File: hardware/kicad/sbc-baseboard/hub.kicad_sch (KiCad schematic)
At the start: 84 parts, among them J1 USB-C upstream, J4 USB-A x2, J5 USB-A x2, U401 USBLC6-2SC6, U402 USB2517, U403 TPS2553DBV, U404 TPS2553DBV, U405 TPS2553DBV, U406 TPS2553DBV, U407 TPS2553DBV, U408 USBLC6-2SC6, U409 USBLC6-2SC6, U410 USBLC6-2SC6, U411 USBLC6-2SC6, Y401 24MHz

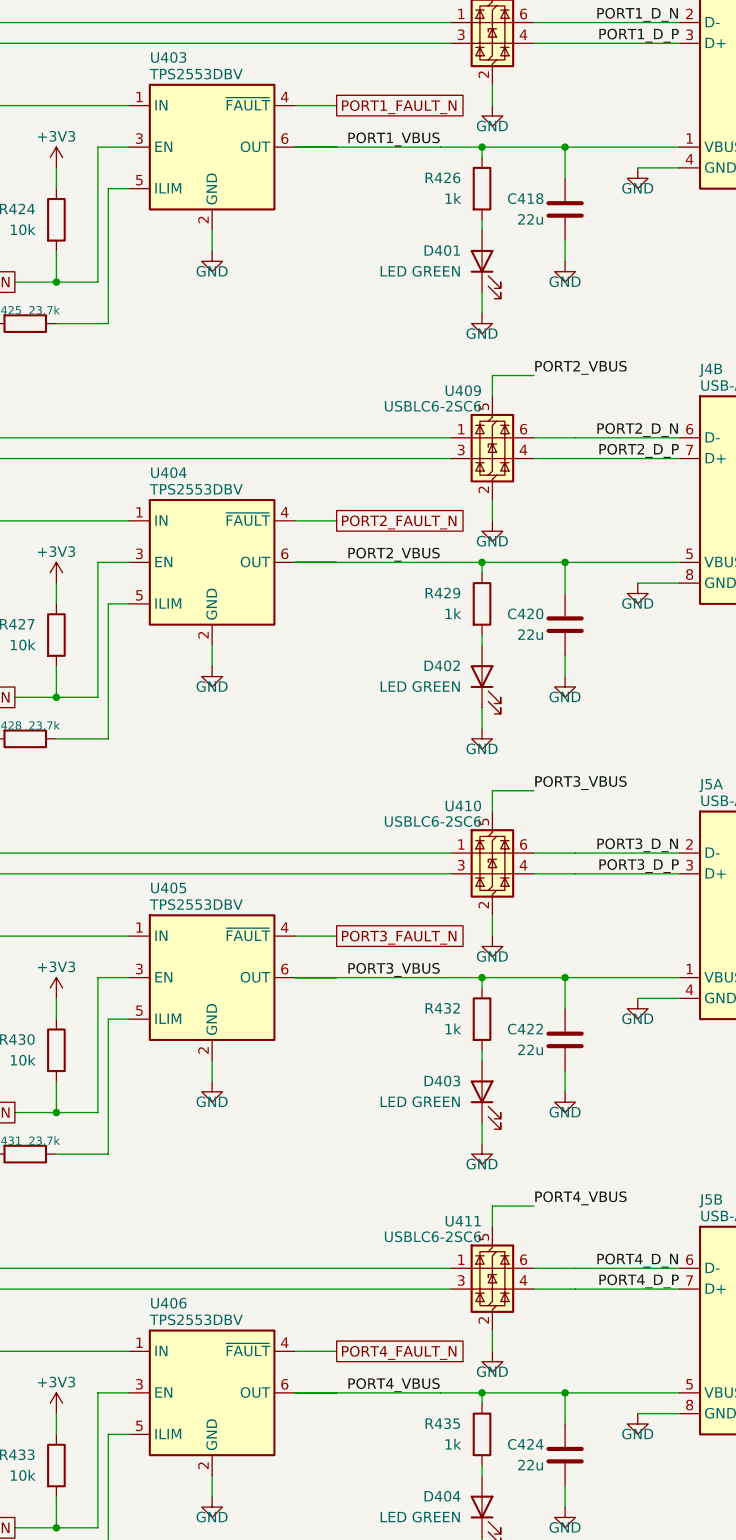
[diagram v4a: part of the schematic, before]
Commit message: Nothing drawn over anything else; FTDI Friend header; DAPLink per FRDM-K64F; 90 ohm USB class
Geometry gate now also reports two wires sharing a stretch, and is at zero on
every sheet. Routes into a stacked connector from one side take staggered
columns and rows; the signal relays are flipped so COM meets the header's
first pin without crossings; the opto-isolator moves above the passthrough
wires and taps the relay's COM lane; a tag before a route ends at the route's
target; routes into joined pins end at the join; the K64's VREGIN diode taps
the VBUS lane beside the ESD's stub; symbol mirrors are applied after
rotation, as KiCad does.

FT231X: the 3V3OUT lane stays on its pin row with its capacitor far out, clear
of the VCC decoupling; J9 mirrors the Adafruit FTDI Friend (VCC 5 V and pin 6
RTS by default on bridged solder jumpers; the first pass had left J9's VCC on
an open jumper only).

DAPLink K20, verified against DAPLink k20dx and the FRDM-K64F OpenSDA circuit:
PTC7 (SWDIO_IN) joins the SWDIO net, 33 R series resistors on the K20's USB
pair (K20_USB_P/N), notes and spec questions 12 and 14 resolved.

USB net class: 0.35 mm / 0.20 mm for 90 ohm on Advanced Circuits' standard
4-layer 62 mil stackup (spec section 8a). ERC 0, geometry 0, merges 0, layout
0, builds reproducible.

Co-Authored-By: Claude Fable 5.1 <noreply@anthropic.com>
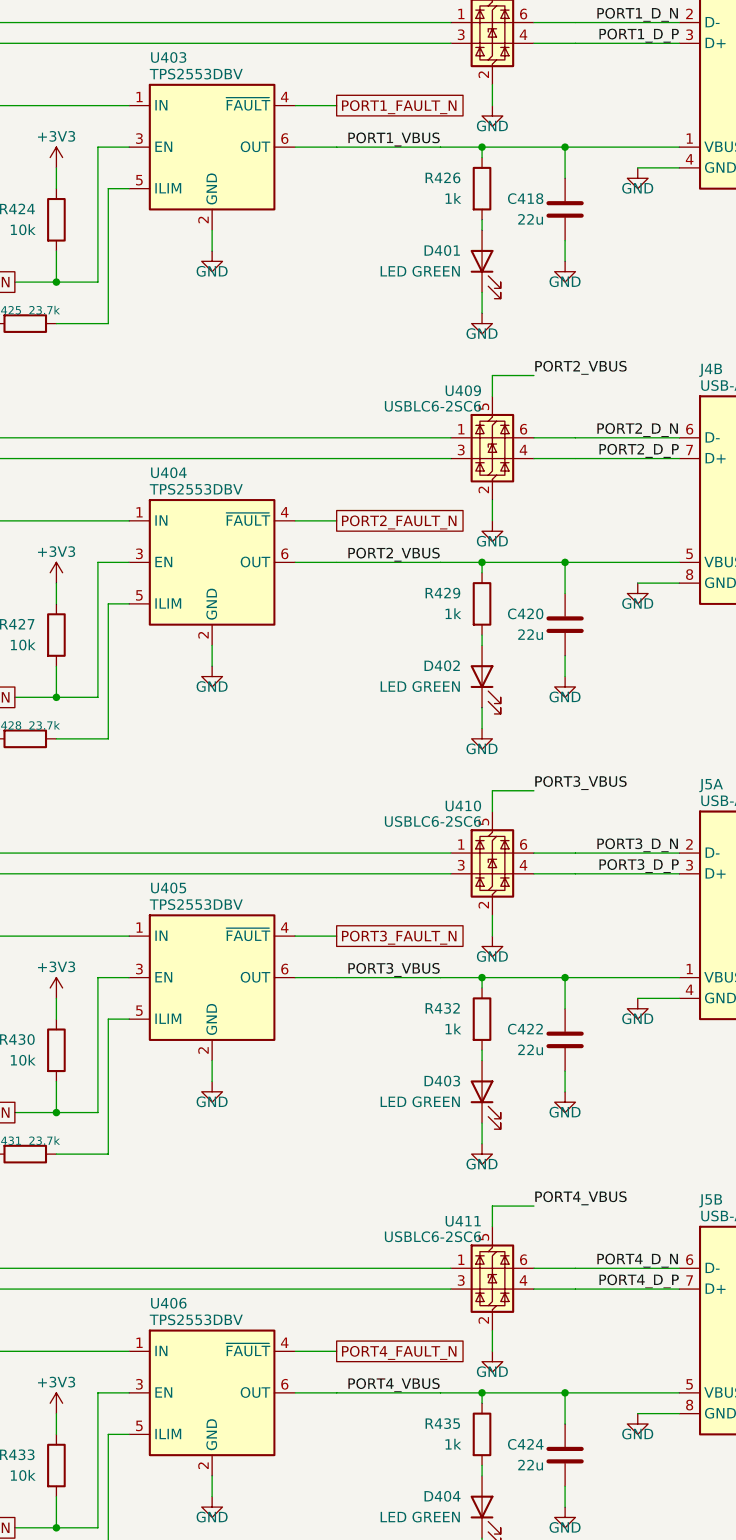
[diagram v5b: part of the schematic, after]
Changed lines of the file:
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@@
 		(pts
 			(xy 355.6 60.96)
-			(xy 337.82 60.96)
-		)
-		(stroke
-			(width 0)
-			(type default)
-		)
-	)
-	(wire
-		(pts
-			(xy 337.82 60.96)
 			(xy 342.9 60.96)
 		)
@@
 		(pts
 			(xy 355.6 111.76)
-			(xy 337.82 111.76)
-		)
-		(stroke
-			(width 0)
-			(type default)
-		)
-	)
-	(wire
-		(pts
-			(xy 337.82 111.76)
 			(xy 342.9 111.76)
 		)
@@
 		(pts
 			(xy 355.6 162.56)
-			(xy 337.82 162.56)
-		)
-		(stroke
-			(width 0)
-			(type default)
-		)
-	)
-	(wire
-		(pts
-			(xy 337.82 162.56)
 			(xy 342.9 162.56)
 		)
@@
 		(pts
 			(xy 355.6 213.36)
-			(xy 337.82 213.36)
-		)
-		(stroke
-			(width 0)
-			(type default)
-		)
-	)
-	(wire
-		(pts
-			(xy 337.82 213.36)
 			(xy 342.9 213.36)
 		)

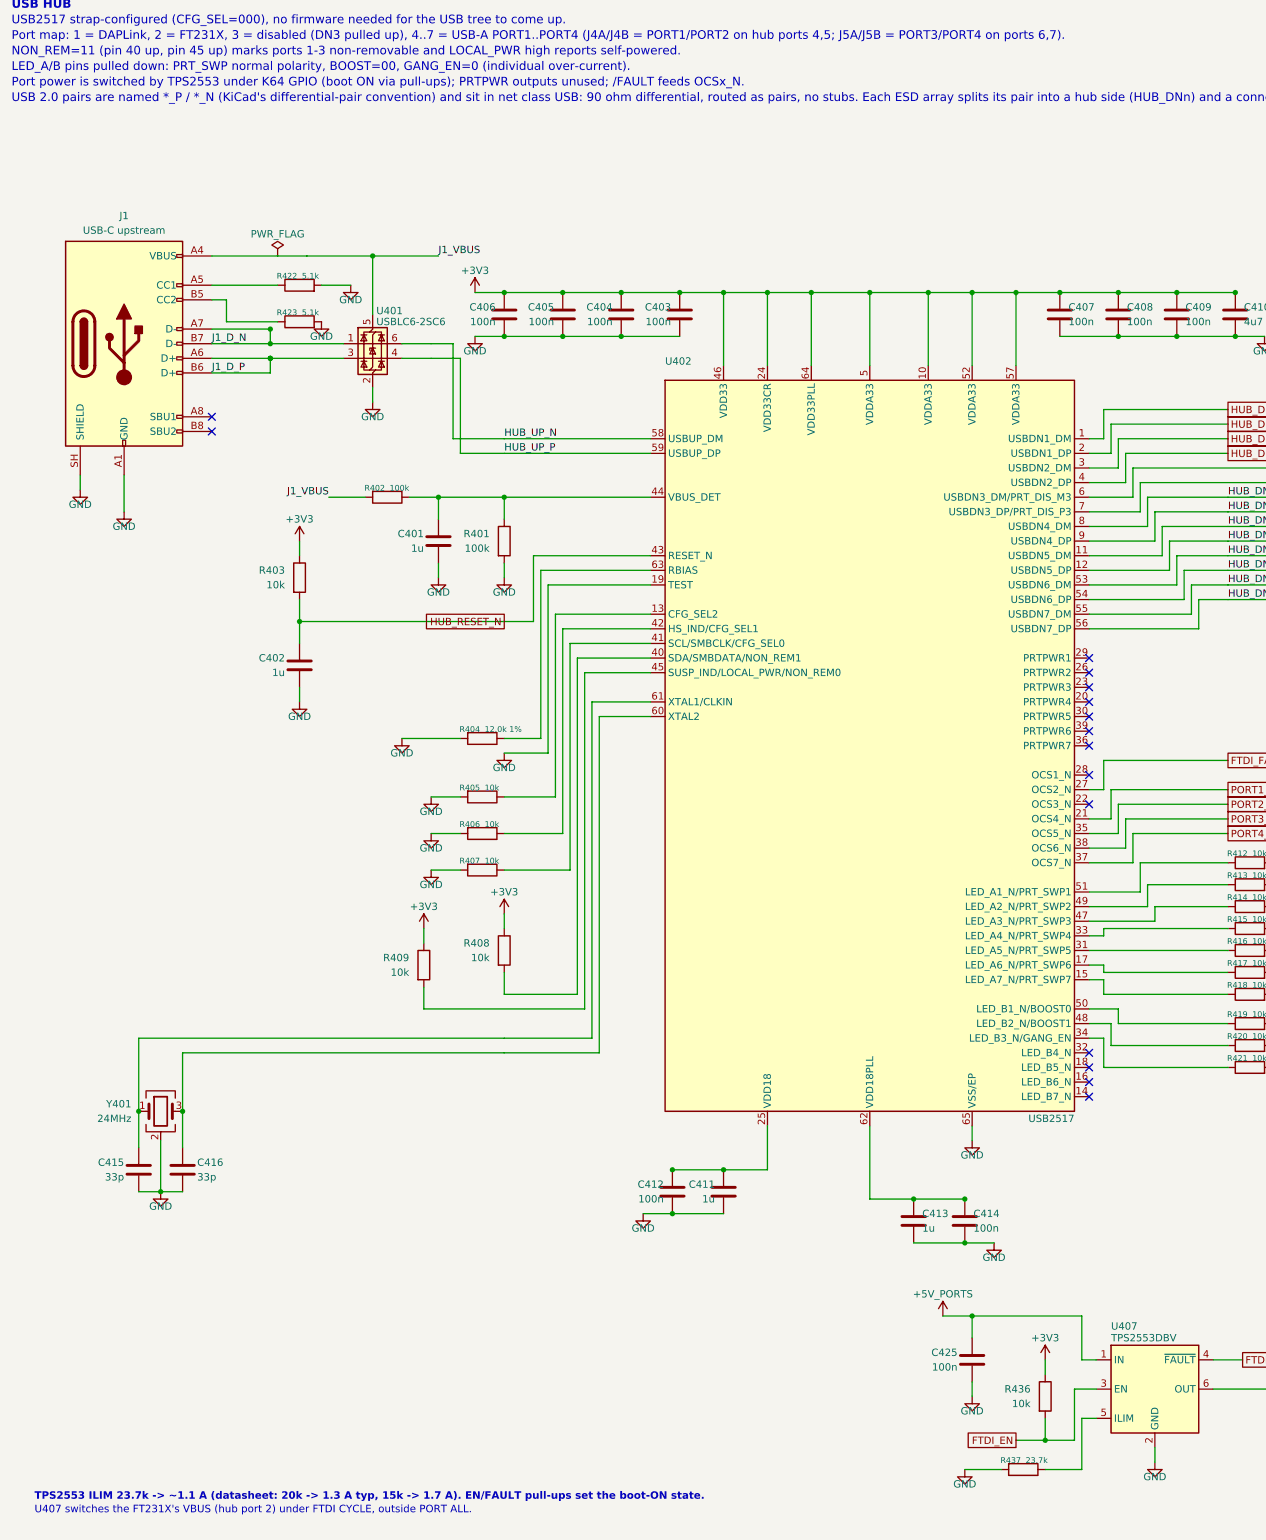
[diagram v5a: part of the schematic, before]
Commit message: Current pathways annotated on the sheets; net classes PSU_3A, USB_VBUS_3A, PWR_6A; layout directives
Net class directive flags on every high-current net, with the class name
carrying the current: the PSU passthrough (PSU_VP, PSU_VOUT, PSU_GND, now
named), the USB port and FTDI VBUS, VBUS_IN, and the +5V_PORTS / +5V_TGT rails
on the power sheet's flag strip. The project file carries the classes with
their widths and patterns; the XML netlist confirms every net's class. Sheet
notes state the currents and widths. Spec: FTDI header section rewritten for
the Adafruit FTDI Friend defaults (a deliberate exception to the back-feed
rule), current-pathway table in 8a. docs/layout-directives.md written from
the spec for the layout generator.

Co-Authored-By: Claude Fable 5.1 <noreply@anthropic.com>
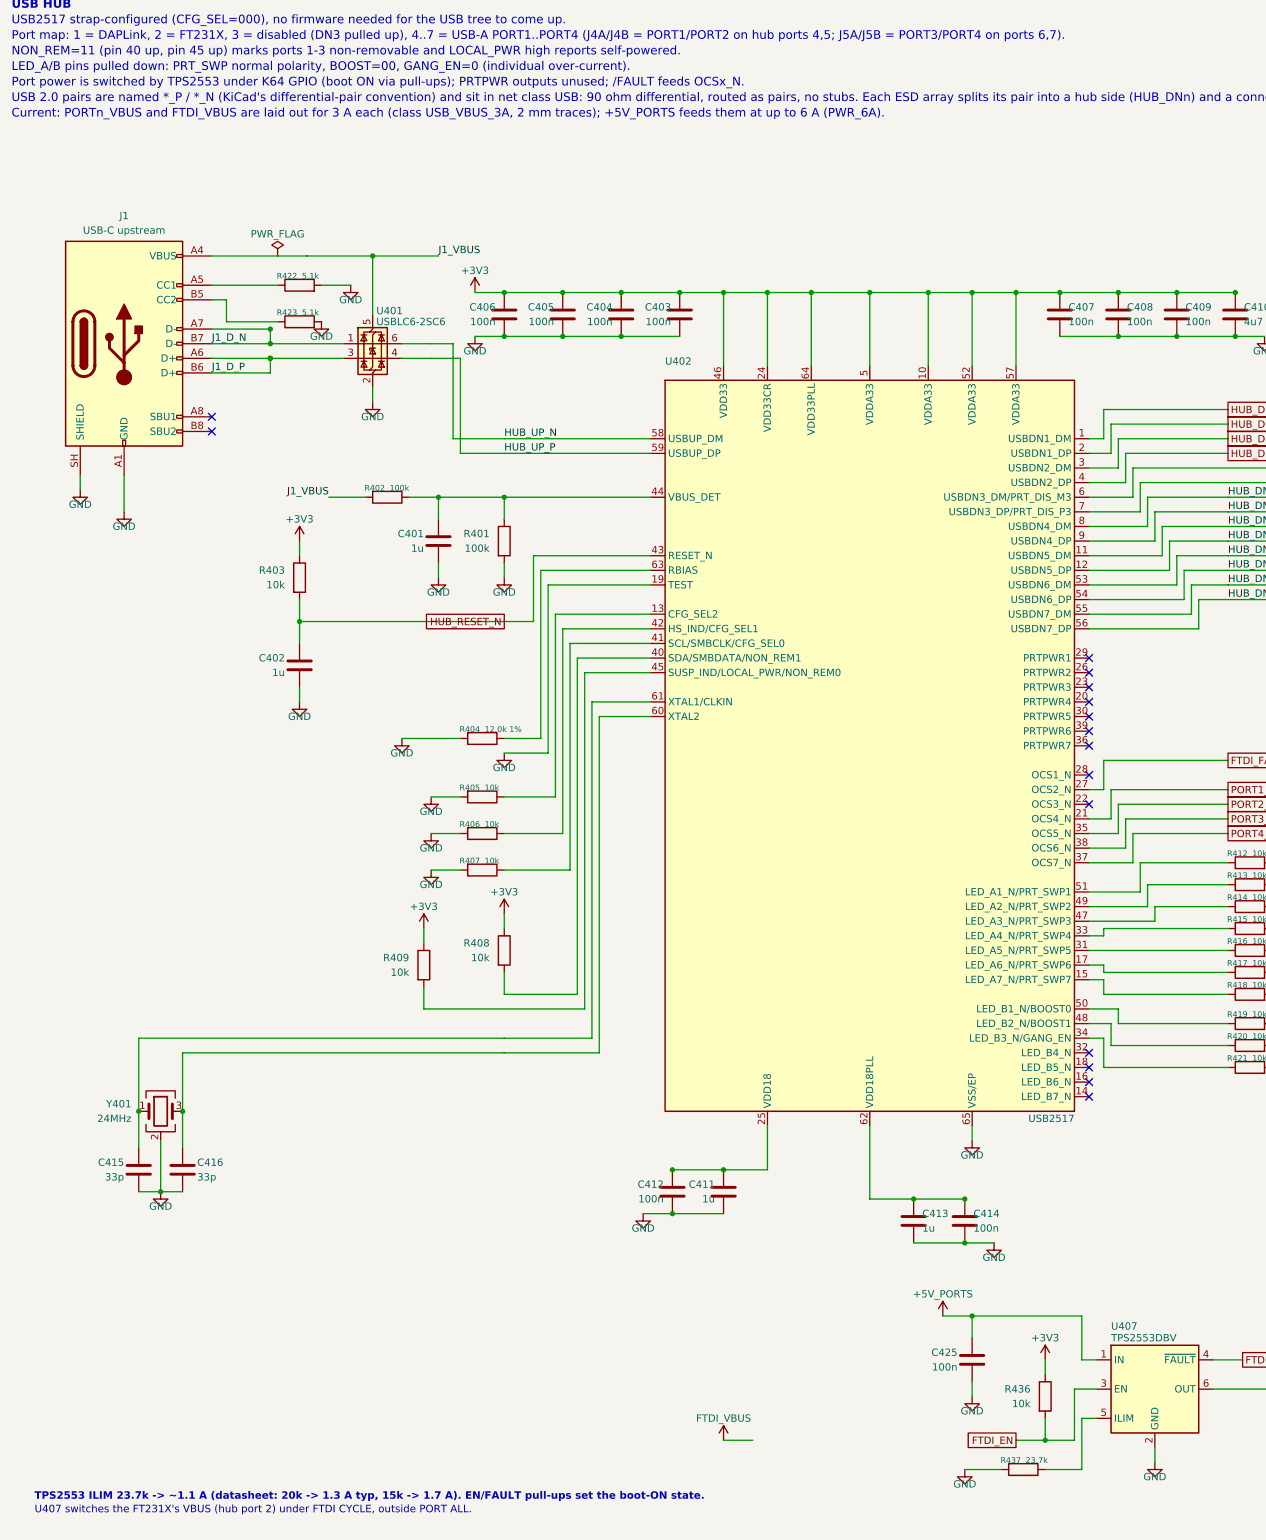
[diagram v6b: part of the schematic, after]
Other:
- note added: "Current: PORTn_VBUS and FTDI_VBUS are laid out for 3 A each (class USB_VBUS_3A, 2 mm traces); +5V_PORTS feeds them at up to 6 A (PWR_6A)."
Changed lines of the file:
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@@
 		)
 	)
+	(text "Current: PORTn_VBUS and FTDI_VBUS are laid out for 3 A each (class USB_VBUS_3A, 2 mm traces); +5V_PORTS feeds them at up to 6 A (PWR_6A)."
+		(exclude_from_sim no)
+		(at 16 35.9 0)
+		(effects
+			(font
+				(size 1.5 1.5)
+			)
+			(justify left bottom)
+		)
+	)
 	(symbol
 		(lib_id "calico-ic:USB2517")
@@
 		)
 	)
+	(netclass_flag ""
+		(length 2.54)
+		(shape round)
+		(at 370.84 60.96 90)
+		(fields_autoplaced no)
+		(effects
+			(font
+				(size 1.27 1.27)
+			)
+			(justify left bottom)
+		)
+		(property "Netclass" "USB_VBUS_3A"
+			(at 371.84 58.12 0)
+			(effects
+				(font
+					(size 1.27 1.27)
+					(italic yes)
+				)
+				(justify left)
+			)
+		)
+	)
 	(wire
 		(pts
@@
 		)
 	)
+	(netclass_flag ""
+		(length 2.54)
+		(shape round)
+		(at 370.84 111.76 90)
+		(fields_autoplaced no)
+		(effects
+			(font
+				(size 1.27 1.27)
+			)
+			(justify left bottom)
+		)
+		(property "Netclass" "USB_VBUS_3A"
+			(at 371.84 108.92 0)
+			(effects
+				(font
+					(size 1.27 1.27)
+					(italic yes)
+				)
+				(justify left)
+			)
+		)
+	)
 	(wire
 		(pts
@@
 		)
 	)
+	(netclass_flag ""
+		(length 2.54)
+		(shape round)
+		(at 370.84 162.56 90)
+		(fields_autoplaced no)
+		(effects
+			(font
+				(size 1.27 1.27)
+			)
+			(justify left bottom)
+		)
+		(property "Netclass" "USB_VBUS_3A"
+			(at 371.84 159.72 0)
+			(effects
+				(font
+					(size 1.27 1.27)
+					(italic yes)
+				)
+				(justify left)
+			)
+		)
+	)
 	(wire
 		(pts
@@
 		)
 	)
+	(netclass_flag ""
+		(length 2.54)
+		(shape round)
+		(at 370.84 213.36 90)
+		(fields_autoplaced no)
+		(effects
+			(font
+				(size 1.27 1.27)
+			)
+			(justify left bottom)
+		)
+		(property "Netclass" "USB_VBUS_3A"
+			(at 371.84 210.52 0)
+			(effects
+				(font
+					(size 1.27 1.27)
+					(italic yes)
+				)
+				(justify left)
+			)
+		)
+	)
 	(wire
 		(pts
@@
 			)
 		)
+	)
+	(symbol
+		(lib_id "power:+3V3")
+		(at 139.7 265.43 0)
+		(unit 1)
+		(body_style 1)
+		(exclude_from_sim no)
+		(in_bom no)
+		(on_board no)
+		(in_pos_files yes)
+		(dnp no)
+		(fields_autoplaced no)
+		(property "Reference" "#PWR05074"
+			(at 139.7 265.43 0)
+			(hide yes)
+			(show_name no)
+			(do_not_autoplace no)
+			(effects
+				(font
+					(size 1.27 1.27)
+				)
+			)
+		)
+		(property "Value" "FTDI_VBUS"
+			(at 139.7 261.62 0)
+			(show_name no)
+			(do_not_autoplace no)
+			(effects
+				(font
+					(size 1.27 1.27)
+				)
+			)
+		)
+		(property "Footprint" ""
+			(at 139.7 265.43 0)
+			(hide yes)
+			(show_name no)
+			(do_not_autoplace no)
+			(effects
+				(font
+					(size 1.27 1.27)
+				)
+			)
+		)
+		(property "Datasheet" "~"
+			(at 139.7 265.43 0)
+			(hide yes)
+			(show_name no)
+			(do_not_autoplace no)
+			(effects
+				(font
+					(size 1.27 1.27)
+				)
+			)
+		)
+		(property "Description" "Power symbol creates a global label with name \"+3V3\""
+			(at 139.7 265.43 0)
+			(hide yes)
+			(show_name no)
+			(do_not_autoplace no)
+			(effects
+				(font
+					(size 1.27 1.27)
+				)
+			)
+		)
+		(pin "1"
+		)
+		(instances
+			(project "sbc-baseboard"
+				(path "/a2d817ed-39de-52b8-83f3-f52a7c9ed802/495ba2f0-b590-56ac-8c98-db51b6e98c32"
+					(reference "#PWR05074")
+					(unit 1)
+				)
+			)
+		)
+	)
+	(wire
+		(pts
+			(xy 139.7 265.43)
+			(xy 144.78 265.43)
+		)
+		(stroke
+			(width 0)
+			(type default)
+		)
+	)
+	(netclass_flag ""
+		(length 2.54)
+		(shape round)
+		(at 144.78 265.43 270)
+		(fields_autoplaced no)
+		(effects
+			(font
+				(size 1.27 1.27)
+			)
+			(justify left bottom)
+		)
+		(property "Netclass" "USB_VBUS_3A"
+			(at 145.78 269.17 0)
+			(effects
+				(font
+					(size 1.27 1.27)
+					(italic yes)
+				)
+				(justify left)
+			)
+		)
